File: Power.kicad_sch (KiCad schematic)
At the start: 15 parts, among them J2 Barrel_Jack_Switch_Pin3Ring, U3 AP2127N-3.3

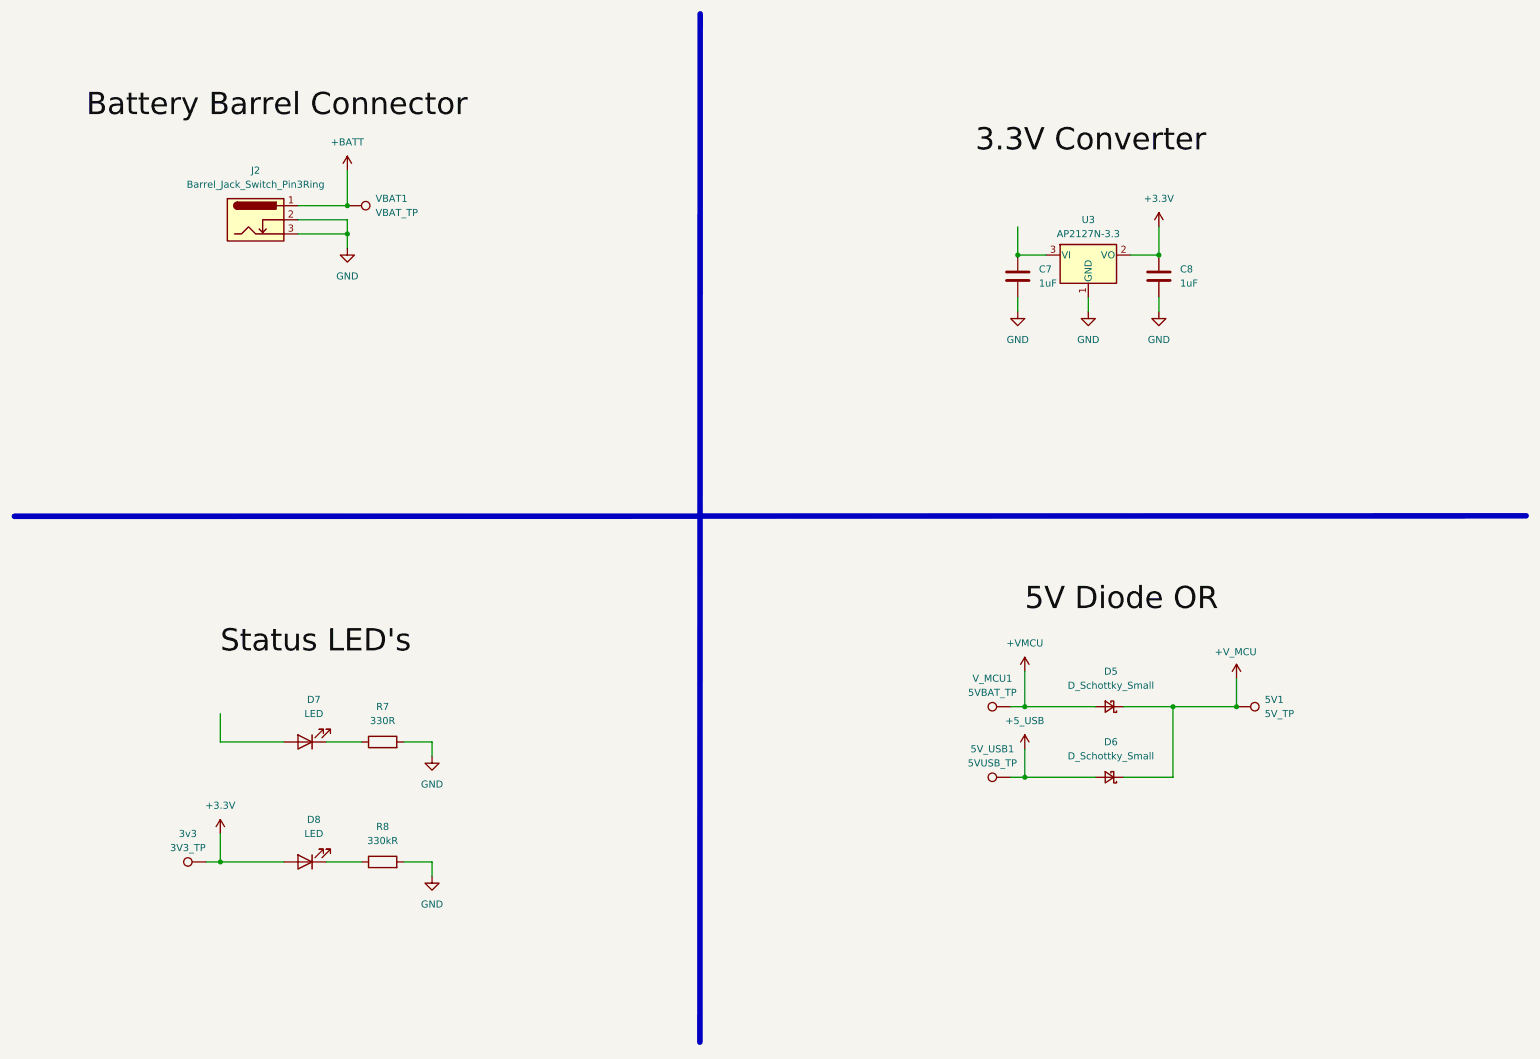
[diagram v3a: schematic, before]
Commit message: Finished PCB routing
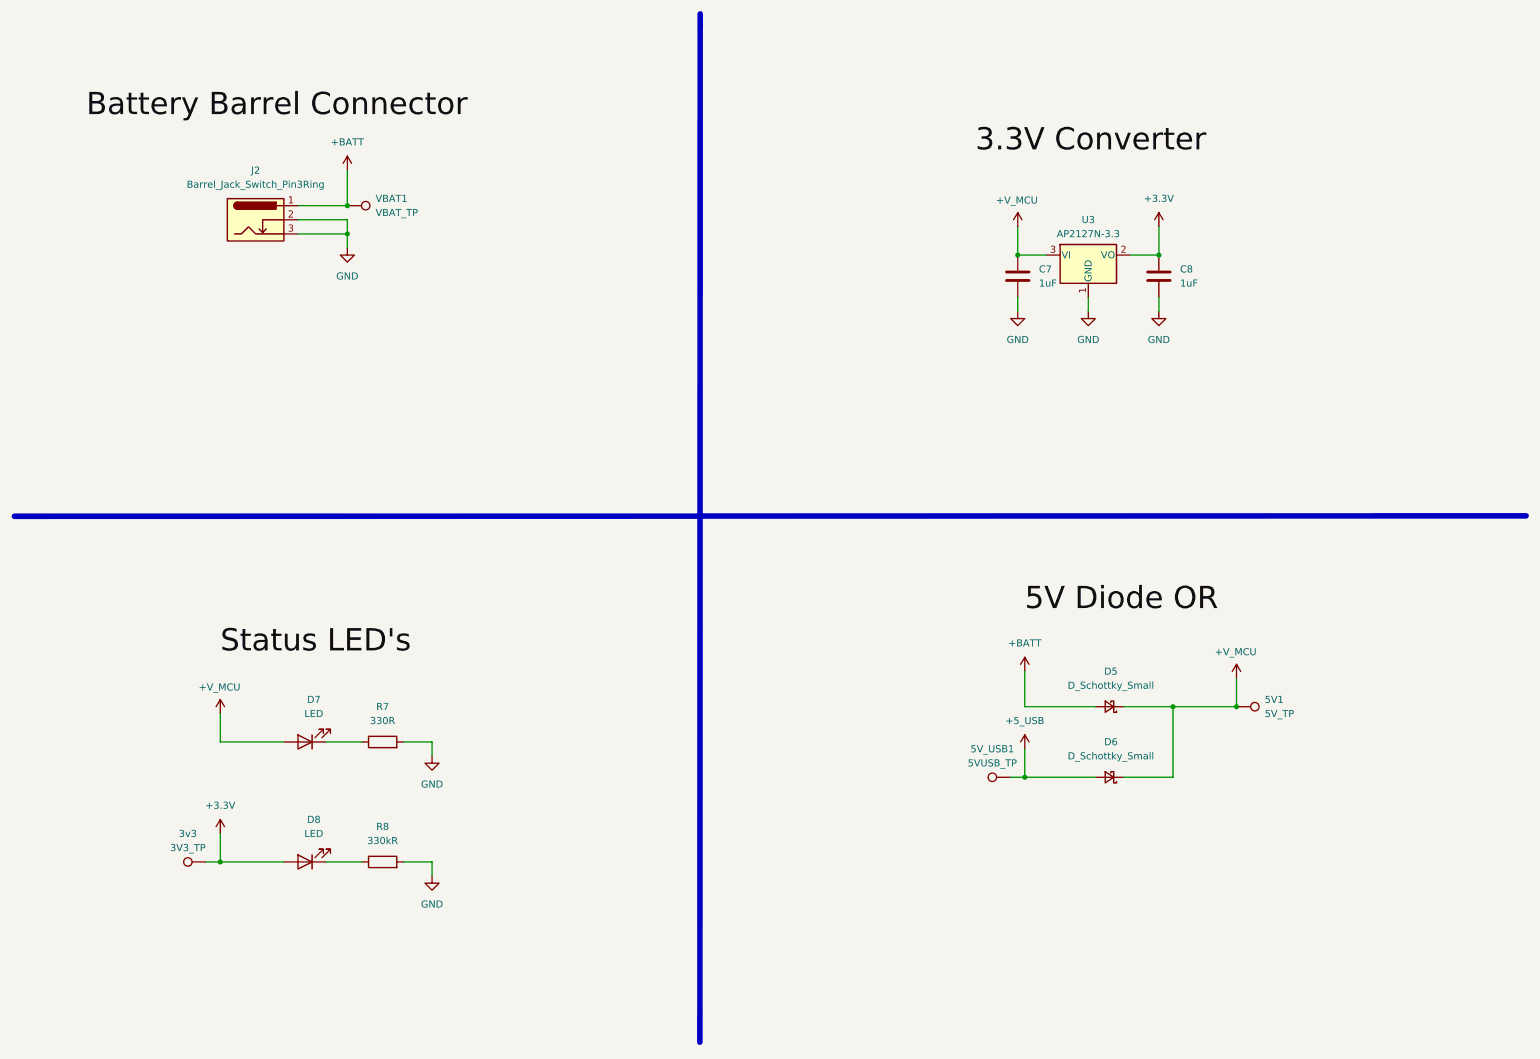
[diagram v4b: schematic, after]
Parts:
- removed V_MCU1: 5VBAT_TP, TestPoint:TestPoint_Pad_D2.0mm, symbol Connector:TestPoint
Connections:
- net +VMCU is gone; now on net +BATT: D5.2 (A)
- net +V_MCU: now also C7.1, D7.2 (A), U3.3 (VI)
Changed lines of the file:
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@@
-	)
-	(junction
-		(at 194.31 137.16)
-		(diameter 0)
-		(color 0 0 0 0)
 	)
 	(junction
@@
 		(pts
 			(xy 213.36 55.88) (xy 218.44 55.88)
-		)
-		(stroke
-			(width 0)
-			(type default)
-		)
-	)
-	(wire
-		(pts
-			(xy 191.77 137.16) (xy 194.31 137.16)
 		)
 		(stroke
@@
 	)
 	(symbol
+		(lib_id "power:+5V")
+		(at 49.53 138.43 0)
+		(unit 1)
+		(exclude_from_sim no)
+		(in_bom yes)
+		(on_board yes)
+		(dnp no)
+		(property "Reference" "#PWR028"
+			(at 49.53 142.24 0)
+			(effects
+				(font
+					(size 1.27 1.27)
+				)
+				(hide yes)
+			)
+		)
+		(property "Value" "+V_MCU"
+			(at 45.6239 133.6603 0)
+			(effects
+				(font
+					(size 1.27 1.27)
+				)
+				(justify left)
+			)
+		)
+		(property "Footprint" ""
+			(at 49.53 138.43 0)
+			(effects
+				(font
+					(size 1.27 1.27)
+				)
+				(hide yes)
+			)
+		)
+		(property "Datasheet" ""
+			(at 49.53 138.43 0)
+			(effects
+				(font
+					(size 1.27 1.27)
+				)
+				(hide yes)
+			)
+		)
+		(property "Description" "Power symbol creates a global label with name \"+5V\""
+			(at 49.53 138.43 0)
+			(effects
+				(font
+					(size 1.27 1.27)
+				)
+				(hide yes)
+			)
+		)
+		(pin "1"
+		)
+		(instances
+			(project "Airboat"
+				(path "/32966cbd-337b-4fa7-b66f-bfe62b1c18c3/bb914a23-e1b8-42c0-8b12-26fadab99985"
+					(reference "#PWR028")
+					(unit 1)
+				)
+			)
+		)
+	)
+	(symbol
+		(lib_id "power:+5V")
+		(at 193.04 50.8 0)
+		(unit 1)
+		(exclude_from_sim no)
+		(in_bom yes)
+		(on_board yes)
+		(dnp no)
+		(property "Reference" "#PWR027"
+			(at 193.04 54.61 0)
+			(effects
+				(font
+					(size 1.27 1.27)
+				)
+				(hide yes)
+			)
+		)
+		(property "Value" "+V_MCU"
+			(at 189.1339 46.0303 0)
+			(effects
+				(font
+					(size 1.27 1.27)
+				)
+				(justify left)
+			)
+		)
+		(property "Footprint" ""
+			(at 193.04 50.8 0)
+			(effects
+				(font
+					(size 1.27 1.27)
+				)
+				(hide yes)
+			)
+		)
+		(property "Datasheet" ""
+			(at 193.04 50.8 0)
+			(effects
+				(font
+					(size 1.27 1.27)
+				)
+				(hide yes)
+			)
+		)
+		(property "Description" "Power symbol creates a global label with name \"+5V\""
+			(at 193.04 50.8 0)
+			(effects
+				(font
+					(size 1.27 1.27)
+				)
+				(hide yes)
+			)
+		)
+		(pin "1"
+		)
+		(instances
+			(project "Airboat"
+				(path "/32966cbd-337b-4fa7-b66f-bfe62b1c18c3/bb914a23-e1b8-42c0-8b12-26fadab99985"
+					(reference "#PWR027")
+					(unit 1)
+				)
+			)
+		)
+	)
+	(symbol
 		(lib_id "Device:D_Schottky_Small")
 		(at 209.55 149.86 180)
@@
 	)
 	(symbol
+		(lib_id "power:+BATT")
+		(at 194.31 130.81 0)
+		(unit 1)
+		(exclude_from_sim no)
+		(in_bom yes)
+		(on_board yes)
+		(dnp no)
+		(fields_autoplaced yes)
+		(property "Reference" "#PWR022"
+			(at 194.31 134.62 0)
+			(effects
+				(font
+					(size 1.27 1.27)
+				)
+				(hide yes)
+			)
+		)
+		(property "Value" "+BATT"
+			(at 194.31 125.73 0)
+			(effects
+				(font
+					(size 1.27 1.27)
+				)
+			)
+		)
+		(property "Footprint" ""
+			(at 194.31 130.81 0)
+			(effects
+				(font
+					(size 1.27 1.27)
+				)
+				(hide yes)
+			)
+		)
+		(property "Datasheet" ""
+			(at 194.31 130.81 0)
+			(effects
+				(font
+					(size 1.27 1.27)
+				)
+				(hide yes)
+			)
+		)
+		(property "Description" "Power symbol creates a global label with name \"+BATT\""
+			(at 194.31 130.81 0)
+			(effects
+				(font
+					(size 1.27 1.27)
+				)
+				(hide yes)
+			)
+		)
+		(pin "1"
+		)
+		(instances
+			(project "Airboat"
+				(path "/32966cbd-337b-4fa7-b66f-bfe62b1c18c3/bb914a23-e1b8-42c0-8b12-26fadab99985"
+					(reference "#PWR022")
+					(unit 1)
+				)
+			)
+		)
+	)
+	(symbol
 		(lib_id "power:+5V")
 		(at 194.31 144.78 0)
@@
 	)
 	(symbol
-		(lib_id "power:+5V")
-		(at 194.31 130.81 0)
-		(unit 1)
-		(exclude_from_sim no)
-		(in_bom yes)
-		(on_board yes)
-		(dnp no)
-		(fields_autoplaced yes)
-		(property "Reference" "#PWR022"
-			(at 194.31 134.62 0)
-			(effects
-				(font
-					(size 1.27 1.27)
-				)
-				(hide yes)
-			)
-		)
-		(property "Value" "+VMCU"
-			(at 194.31 125.73 0)
-			(effects
-				(font
-					(size 1.27 1.27)
-				)
-			)
-		)
-		(property "Footprint" ""
-			(at 194.31 130.81 0)
-			(effects
-				(font
-					(size 1.27 1.27)
-				)
-				(hide yes)
-			)
-		)
-		(property "Datasheet" ""
-			(at 194.31 130.81 0)
-			(effects
-				(font
-					(size 1.27 1.27)
-				)
-				(hide yes)
-			)
-		)
-		(property "Description" "Power symbol creates a global label with name \"+5V\""
-			(at 194.31 130.81 0)
-			(effects
-				(font
-					(size 1.27 1.27)
-				)
-				(hide yes)
-			)
-		)
-		(pin "1"
-		)
-		(instances
-			(project "Airboat"
-				(path "/32966cbd-337b-4fa7-b66f-bfe62b1c18c3/bb914a23-e1b8-42c0-8b12-26fadab99985"
-					(reference "#PWR022")
-					(unit 1)
-				)
-			)
-		)
-	)
-	(symbol
 		(lib_id "power:+BATT")
 		(at 72.39 40.64 0)
@@
 					(unit 1)
 				)
-			)
-		)
-	)
-	(symbol
-		(lib_id "Connector:TestPoint")
-		(at 191.77 137.16 90)
-		(unit 1)
-		(exclude_from_sim no)
-		(in_bom yes)
-		(on_board yes)
-		(dnp no)
-		(fields_autoplaced yes)
-		(property "Reference" "V_MCU1"
-			(at 188.468 132.08 90)
-			(effects
-				(font
-					(size 1.27 1.27)
-				)
-			)
-		)
-		(property "Value" "5VBAT_TP"
-			(at 188.468 134.62 90)
-			(effects
-				(font
-					(size 1.27 1.27)
-				)
-			)
-		)
-		(property "Footprint" "TestPoint:TestPoint_Pad_D2.0mm"
-			(at 191.77 132.08 0)
-			(effects
-				(font
-					(size 1.27 1.27)
-				)
-				(hide yes)
-			)
-		)
-		(property "Datasheet" "~"
-			(at 191.77 132.08 0)
-			(effects
-				(font
-					(size 1.27 1.27)
-				)
-				(hide yes)
-			)
-		)
-		(property "Description" "test point"
-			(at 191.77 137.16 0)
-			(effects
-				(font
-					(size 1.27 1.27)
-				)
-				(hide yes)
-			)
-		)
-		(pin "1"
-		)
-		(instances
-			(project "Airboat"
-				(path "/32966cbd-337b-4fa7-b66f-bfe62b1c18c3/bb914a23-e1b8-42c0-8b12-26fadab99985"
-					(reference "V_MCU1")
-					(unit 1)
-				)

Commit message: Updated PCB to be smaller and support stepper
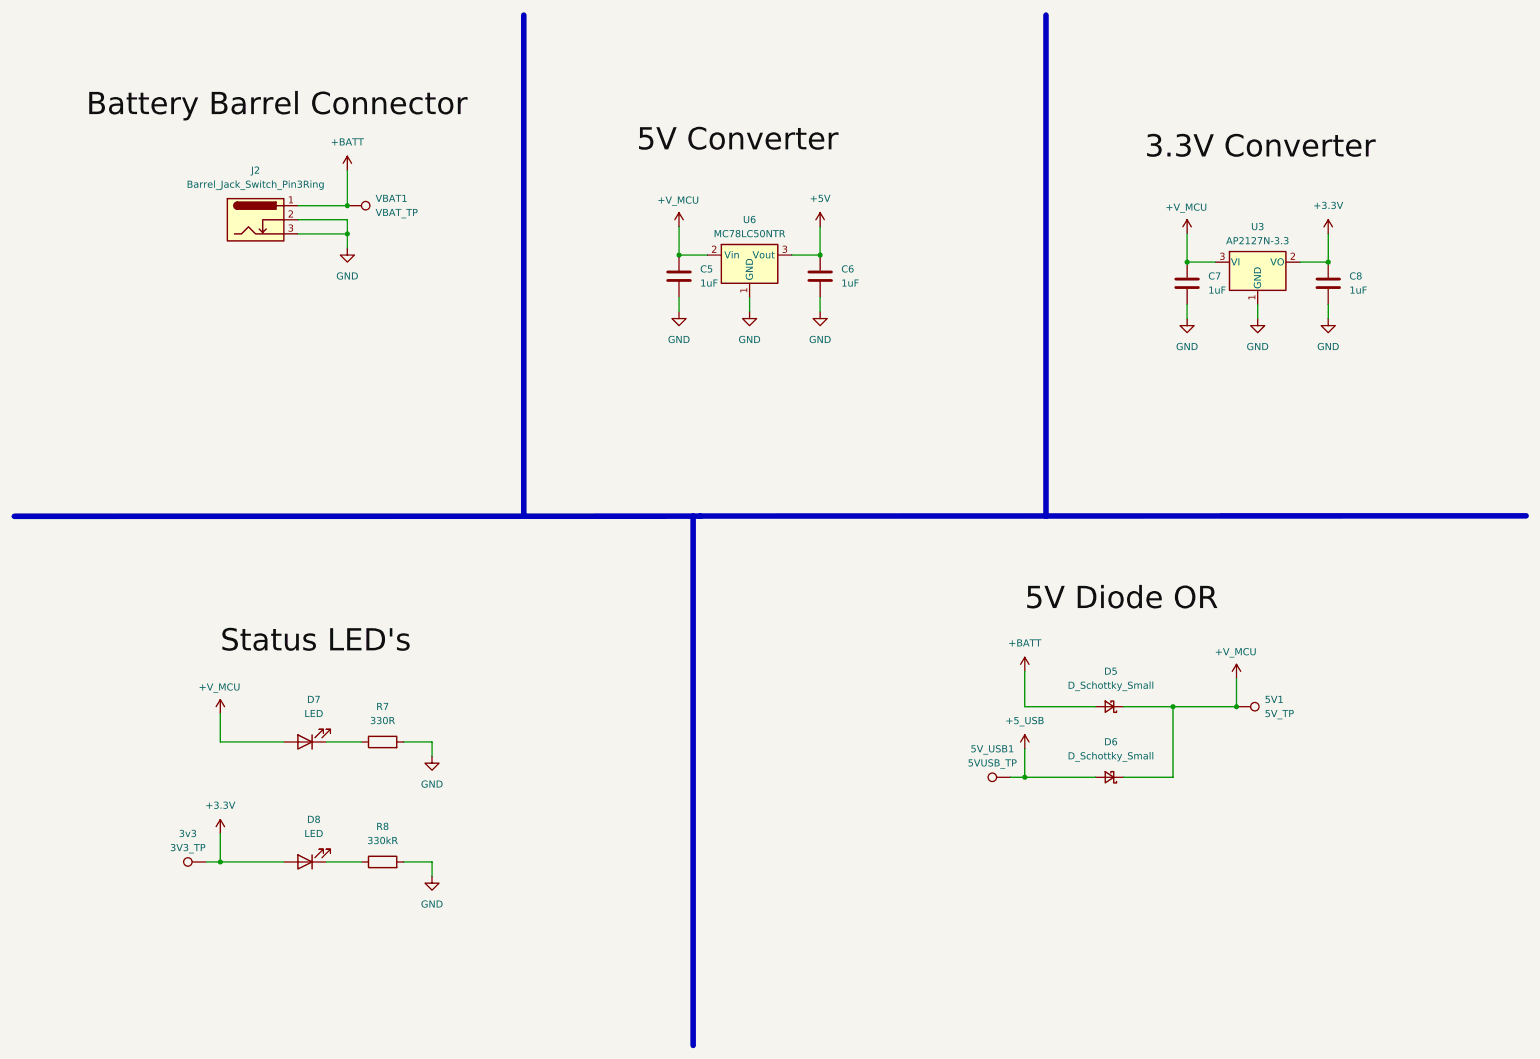
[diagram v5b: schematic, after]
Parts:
- added C5, C6: 1uF, Capacitor_SMD:C_0603_1608Metric_Pad1.08x0.95mm_HandSolder, symbol Device:C
- added U6: MC78LC50NTR, Package_TO_SOT_SMD:SOT-23-5, symbol Regulator_Linear:MC78LC50NTR
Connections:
- net +V_MCU: now also C5.1, U6.2 (Vin)
- net GND: now also C5.2, C6.2, U6.1 (GND)
- new net +5V: C6.1, U6.3 (Vout)
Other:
- moved on the sheet: C7, C8, U3
